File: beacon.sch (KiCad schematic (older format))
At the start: 38 parts

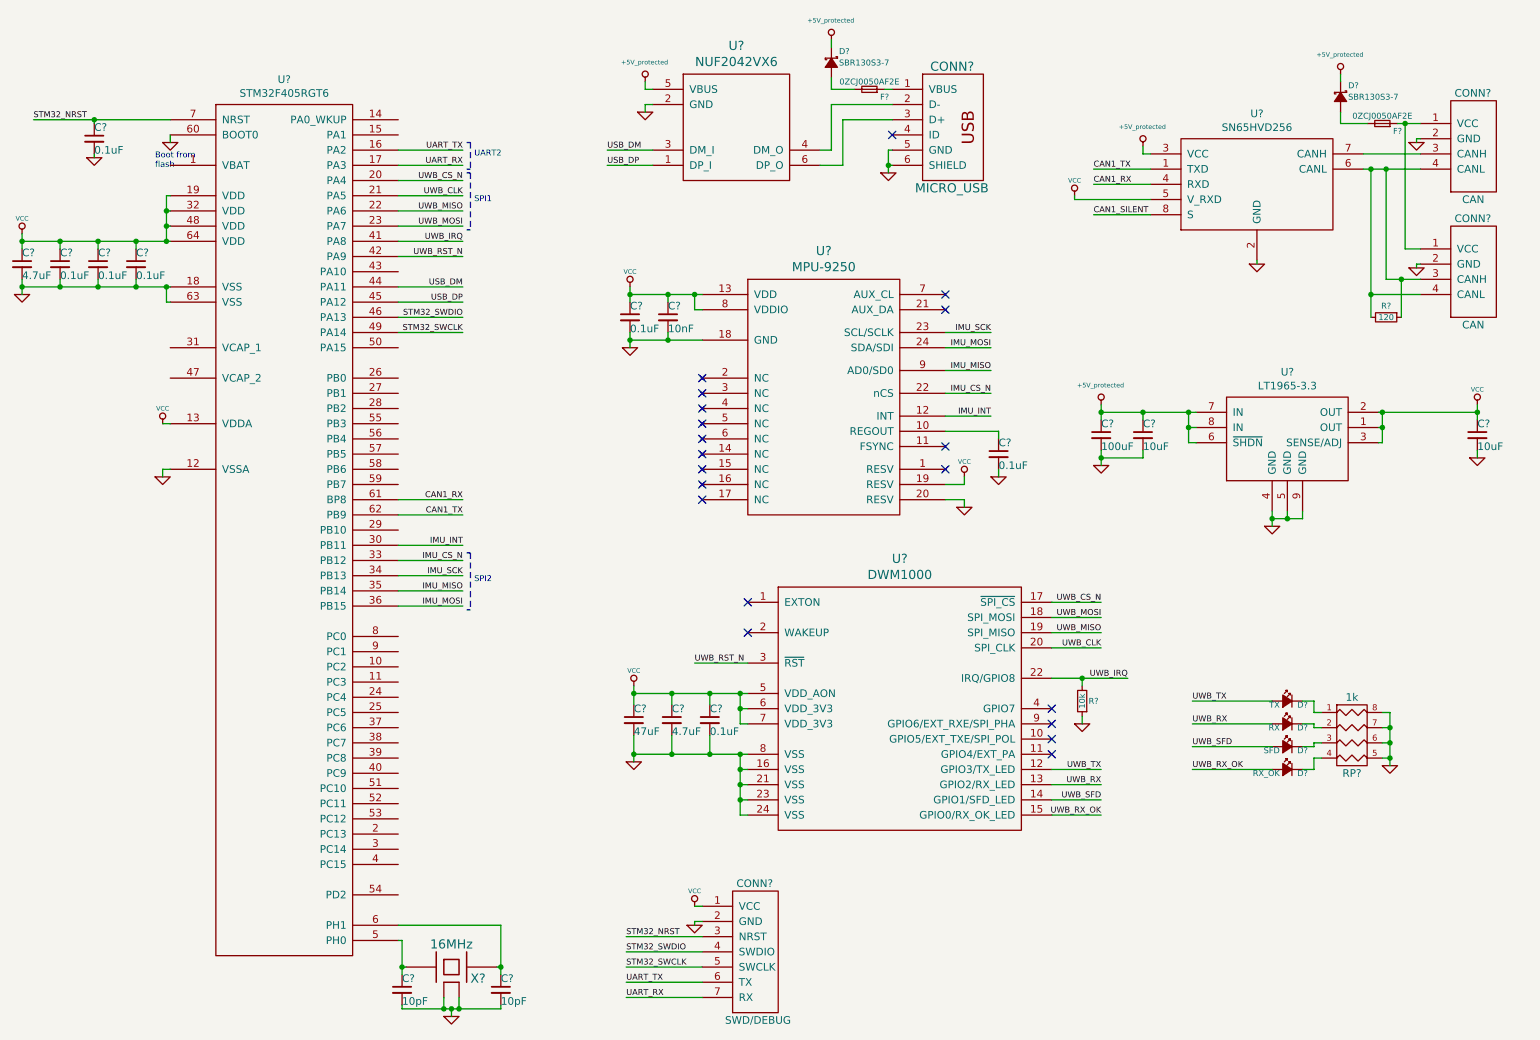
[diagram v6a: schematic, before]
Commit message: Add debug leds, logo & plot pdf
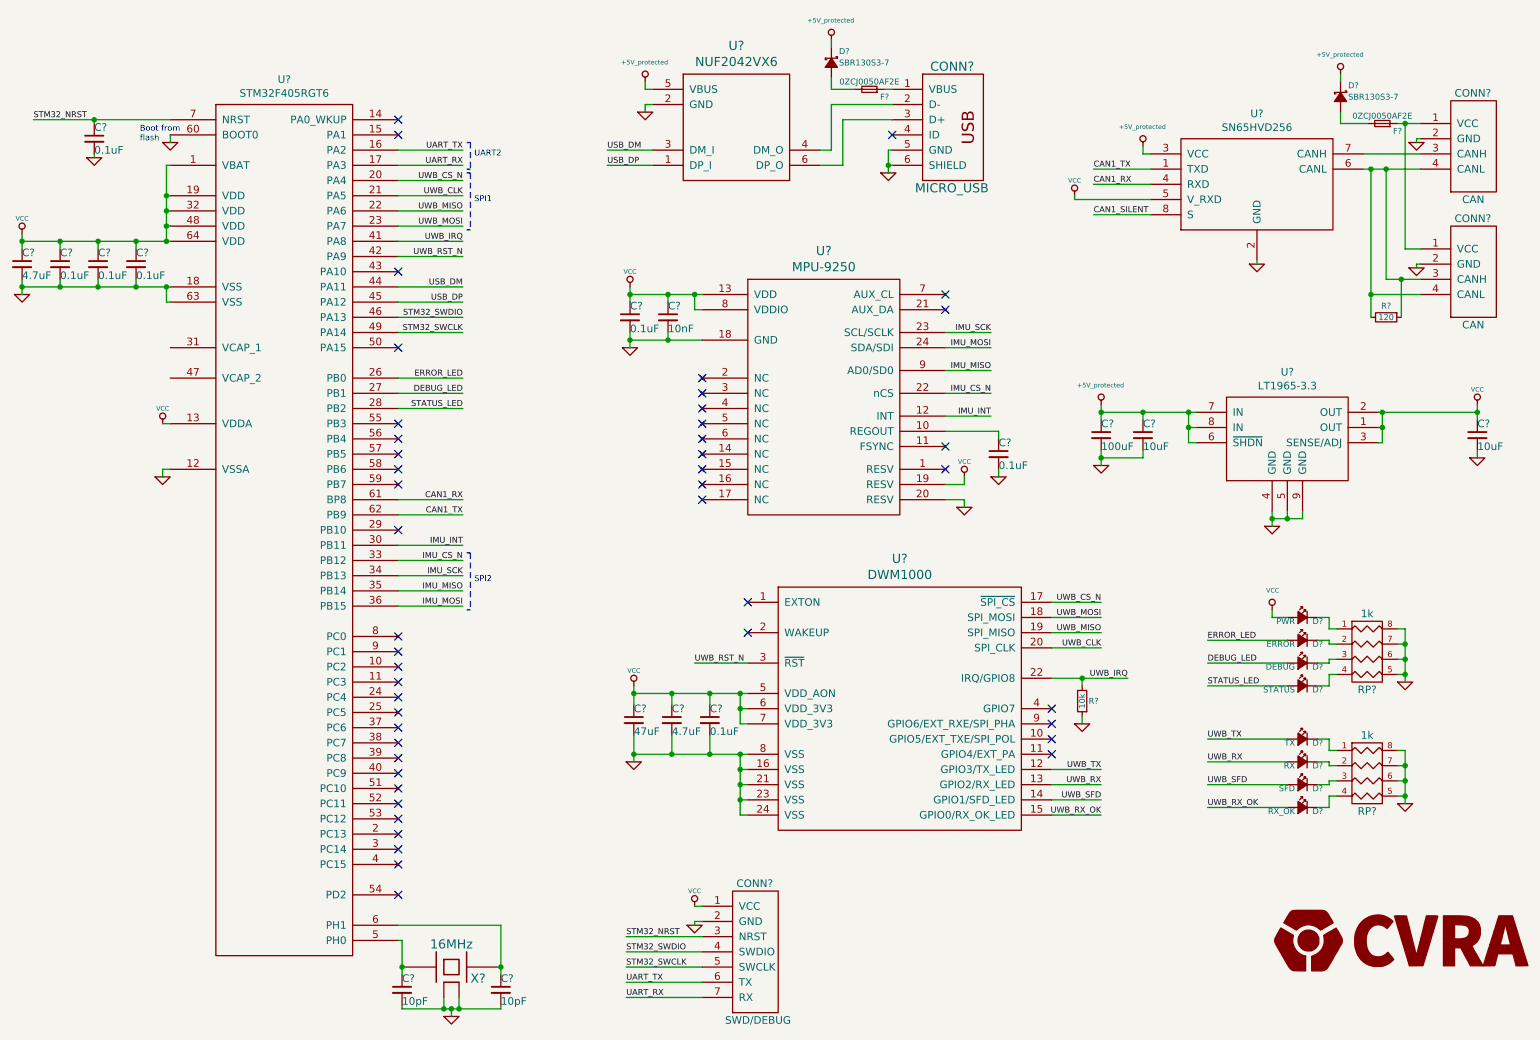
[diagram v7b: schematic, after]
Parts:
- added D?: PWR, symbol Led_Small
- added D?: ERROR, symbol Led_Small
- added D?: DEBUG, symbol Led_Small
- added D?: STATUS, symbol Led_Small
- added RP?: 1k, symbol R_PACK4
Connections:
- net GND: now also RP?.5 (R4), RP?.6 (R3), RP?.7 (R2), RP?.8 (R1)
- net VCC: now also U?.1 (VBAT), D?.2 (A)
- net ERROR_LED: now reaches U?.26 (PB0)
- net ERROR_LED: now also D?.2 (A)
- net DEBUG_LED: now reaches U?.27 (PB1)
- net DEBUG_LED: now also D?.2 (A)
- net STATUS_LED: now reaches U?.28 (PB2)
- net STATUS_LED: now also D?.2 (A)
- new net: D?.1 (K), RP?.1 (P1)
- new net: D?.1 (K), RP?.2 (P2)
- new net: D?.1 (K), RP?.3 (P3)
- new net: D?.1 (K), RP?.4 (P4)
- no-connect marks 20 -> 47
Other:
- moved on the sheet: D?, RP?

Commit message: Annotate schematic
Also added missing capacitors on MCU
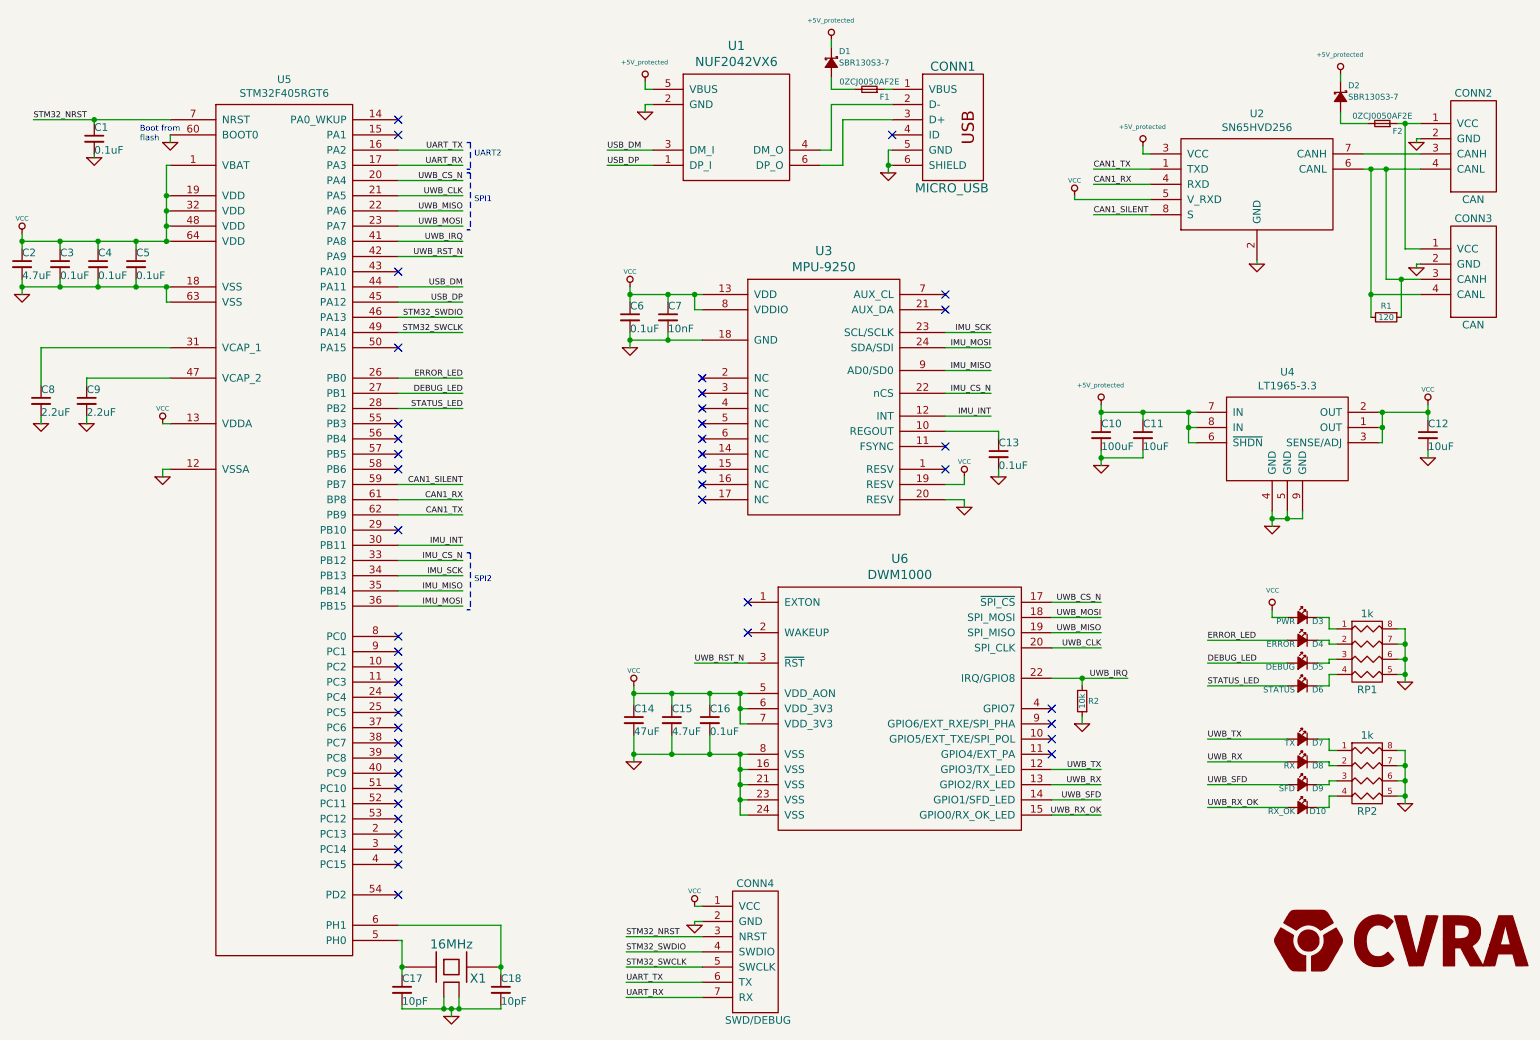
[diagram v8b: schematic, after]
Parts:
- added C8, C9: 2.2uF, symbol C_Small
- gave numbers to parts that had none: 43
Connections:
- net CAN1_SILENT: now also U5.59 (PB7)
- net GND: now also C8.2, C9.2
- net at U5.31 (VCAP_1): now also C8.1
- net at U5.47 (VCAP_2): now also C9.1
- no-connect marks 47 -> 46
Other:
- moved on the sheet: C12
